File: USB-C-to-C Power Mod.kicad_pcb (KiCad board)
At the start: 2 copper layers, 7.8 x 8.7 mm, 12 parts, among them J1 CC1, J2 CC2

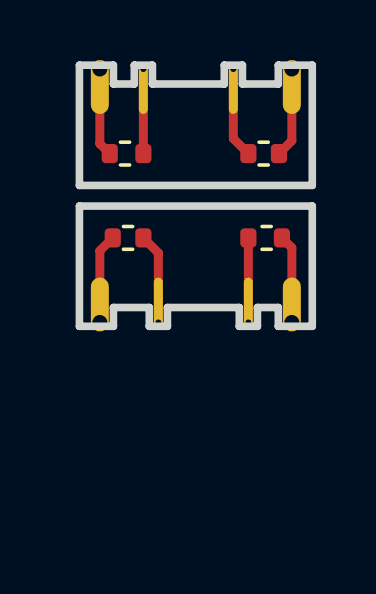
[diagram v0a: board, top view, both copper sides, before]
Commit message: initial modification to 6pin design now awaiting oshpark prototypes
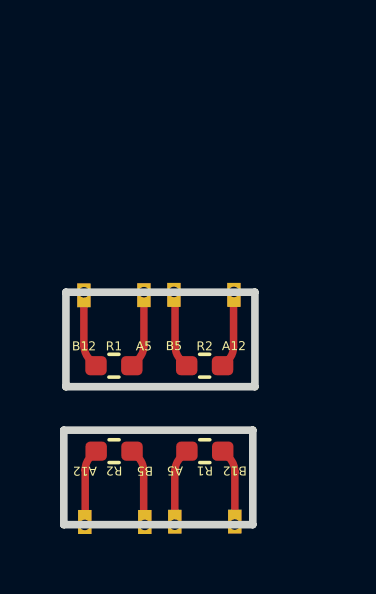
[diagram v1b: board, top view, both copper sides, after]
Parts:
- removed GND (x4): GND, FlexPCB:Plated_Hole_D0.6mm
- removed the J1 at (142.9, 95.4)
- removed the J1 at (146.8, 92.9)
- removed the J2 at (149.2, 95.4)
- removed the J2 at (140.6, 92.9)
- removed the R1 at (142.6, 95.5)
- removed the R1 at (147.1, 92.7)
- removed the R2 at (147.2, 95.5)
- removed the R2 at (142.5, 92.7)
- added J1: A5, FlexPCB:Plated_Hole_D0.3mm, F.Cu at (141.9, 103.8)
- added J1: A5, FlexPCB:Plated_Hole_D0.3mm, F.Cu at (145.4, 98.6)
- added J2: B5, FlexPCB:Plated_Hole_D0.3mm, F.Cu at (146.4, 98.6)
- added J2: B5, FlexPCB:Plated_Hole_D0.3mm, F.Cu at (140.9, 103.8)
- added J3: B12, FlexPCB:Plated_Hole_D0.3mm, F.Cu at (143.4, 98.6)
- added J3: B12, FlexPCB:Plated_Hole_D0.3mm, F.Cu at (143.9, 103.8)
- added J4: A12, FlexPCB:Plated_Hole_D0.3mm, F.Cu at (138.9, 103.8)
- added J4: A12, FlexPCB:Plated_Hole_D0.3mm, F.Cu at (148.4, 98.6)
- added R1: 5.1K, Resistor_SMD:R_0402_1005Metric_Pad0.72x0.64mm_HandSolder, F.Cu at (142.2, 99.8)
- added R1: 5.1K, Resistor_SMD:R_0402_1005Metric_Pad0.72x0.64mm_HandSolder, F.Cu at (145.2, 102.6)
- added R2: 5.1K, Resistor_SMD:R_0402_1005Metric_Pad0.72x0.64mm_HandSolder, F.Cu at (142.2, 102.6)
- added R2: 5.1K, Resistor_SMD:R_0402_1005Metric_Pad0.72x0.64mm_HandSolder, F.Cu at (145.2, 99.8)
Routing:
- net GND: track 11.9 -> 0.00 mm
- net Net-(J4-Pad1): track 0.00 -> 4.70 mm
- net Net-(J3-Pad1): track 0.00 -> 4.66 mm
- net Net-(J1-Pad1): track 6.05 -> 4.66 mm
- net Net-(J2-Pad1): track 5.64 -> 4.65 mm
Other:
- board size 7.8 x 8.7 mm -> 6.4 x 7.7 mm
- net class Default removed
- rule pad_to_mask_clearance: 0 -> 0.0508
- board text added: "USB C2C 6pin Randomblock1"
- board text removed: "USB C2C [ide]"

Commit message: made solder pads bigger, add 0602 version
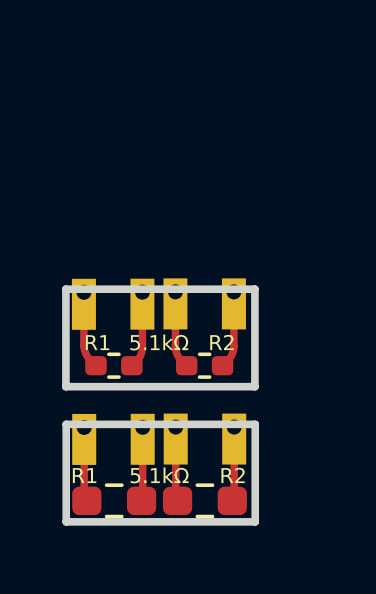
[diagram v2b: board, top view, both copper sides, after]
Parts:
- R1, R2: footprint Resistor_SMD:R_0402_1005Metric_Pad0.72x0.64mm_HandSolder -> Resistor_SMD:R_0603_1608Metric_Pad0.98x0.95mm_HandSolder
- moved J4 9.61 mm to (148.5, 103.1), turned to -90 degrees
- moved J2 5.68 mm to (146.5, 103.1), turned to -90 degrees
- moved J1 3.60 mm to (145.4, 103.1), turned to -90 degrees
- moved R2 3.45 mm to (145.2, 104.3), turned to 0 degrees
- moved R1 3.44 mm to (142.2, 104.3), turned to 0 degrees
- moved J3 0.81 mm to (143.5, 103.1), turned to -90 degrees
- moved J2 0.05 mm to (146.5, 98.6)
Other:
- board size 6.4 x 7.7 mm -> 6.3 x 7.8 mm
- board text added: "0403"
- board text added: "0603"
- board text added: "5.1kΩ"
